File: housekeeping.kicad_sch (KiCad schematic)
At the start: 9 parts, among them U15 LMR43620MSC5RPERQ1

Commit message: Adding control stuff
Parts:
- removed C74: C, symbol Device:C
- removed R72: 49.9k, symbol Device:R_US
- removed R73: 12.4k, symbol Device:R_US
- added C74, C76: 22uF, Capacitor_SMD:CP_Elec_6.3x5.9, symbol Device:C_Polarized_US
- C70: value 0.1uF -> 100nF; footprint (none) -> Capacitor_SMD:C_0603_1608Metric; Mfr (none) -> KYOCERA AVX; Mfr P/N (none) -> 06035C104K4T2A; Supplier_1 (none) -> Digikey; Supplier_1 P/N (none) -> 478-KAM15AR71H104KTTR-ND; Supplier_1 Price @ Qty (none) -> 1; Supplier_1 Unit Price (none) -> 0.10000
- C71: footprint (none) -> Capacitor_SMD:C_0805_2012Metric; Mfr (none) -> Murata Electronics; Mfr P/N (none) -> GCM21BR71H105KA03K; Supplier_1 (none) -> Digikey; Supplier_1 P/N (none) -> 490-13310-2-ND; Supplier_1 Price @ Qty (none) -> 1; Supplier_1 Unit Price (none) -> 0.22000
- C72: footprint (none) -> Capacitor_SMD:C_0805_2012Metric; Mfr (none) -> Murata Electronics; Mfr P/N (none) -> GRT21BR61H475KE13L; Supplier_1 (none) -> Digikey; Supplier_1 P/N (none) -> 490-12394-2-ND; Supplier_1 Price @ Qty (none) -> 1; Supplier_1 Unit Price (none) -> 0.24000
- C73: footprint (none) -> Capacitor_SMD:C_0603_1608Metric; Mfr (none) -> KYOCERA AVX; Mfr P/N (none) -> 06035C104K4T2A; Supplier_1 (none) -> Digikey; Supplier_1 P/N (none) -> 478-KAM15AR71H104KTTR-ND; Supplier_1 Price @ Qty (none) -> 1; Supplier_1 Unit Price (none) -> 0.10000
- L2: footprint (none) -> Inductor_SMD:L_Bourns_SRN6045TA; Mfr (none) -> Bourns Inc.; Mfr P/N (none) -> SRN6045TA-3R3Y; Supplier_1 (none) -> Digikey; Supplier_1 P/N (none) -> SRN6045TA-3R3YTR-ND; Supplier_1 Price @ Qty (none) -> 1; Supplier_1 Unit Price (none) -> 0.45000
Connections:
- net +5V: now also U15.8 (VOUT_BIAS), C74.1, C76.1
- net GND: now also U15.1 (MODE_SYNC), C74.2, C76.2
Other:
- moved on the sheet: C71, C72, L2, U15

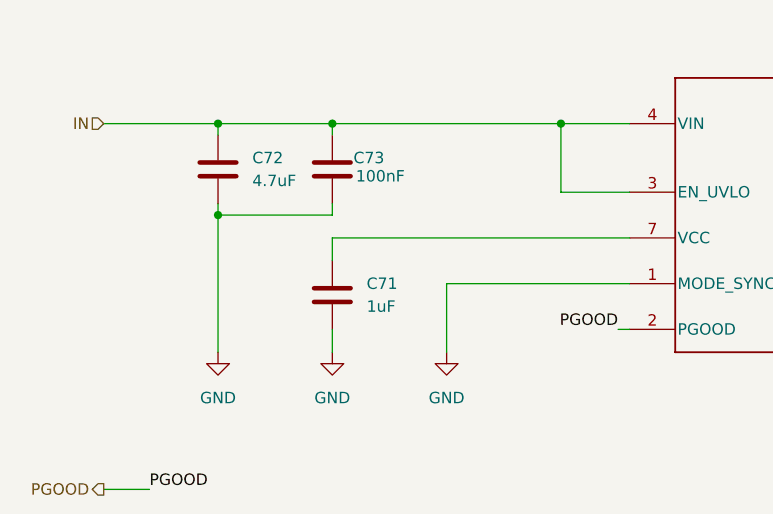
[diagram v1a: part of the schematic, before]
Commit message: Adding in connections to schematic
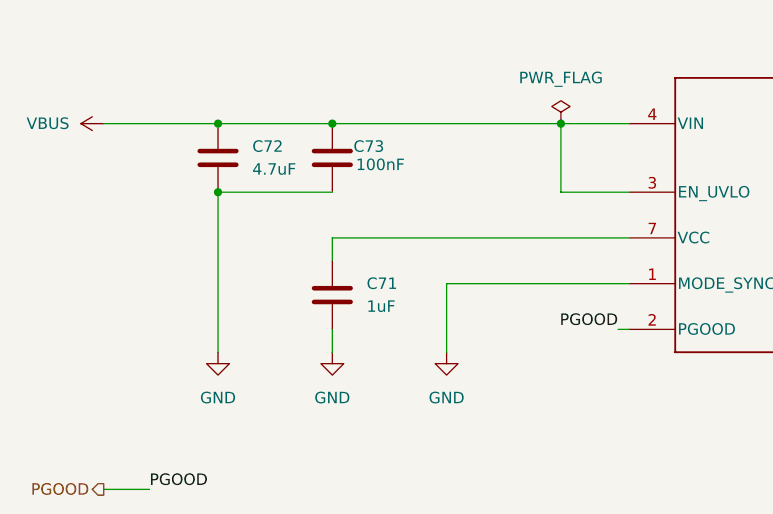
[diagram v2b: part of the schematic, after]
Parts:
- U15: footprint RPE0009A-MFG -> _Power_Board:RPE0009A-MFG
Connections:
- net IN renamed VBUS
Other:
- moved on the sheet: C72, C73
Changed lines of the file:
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@@
+	)
+	(junction
+		(at 58.42 99.06)
+		(diameter 0)
+		(color 0 0 0 0)
 	)
 	(junction
@@
 	)
 	(junction
-		(at 58.42 101.6)
-		(diameter 0)
-		(color 0 0 0 0)
-	)
-	(junction
 		(at 229.87 91.44)
 		(diameter 0)
@@
 	(wire
 		(pts
-			(xy 58.42 100.33) (xy 58.42 101.6)
+			(xy 58.42 99.06) (xy 58.42 116.84)
 		)
 		(stroke
@@
 	(wire
 		(pts
-			(xy 58.42 91.44) (xy 58.42 92.71)
-		)
-		(stroke
-			(width 0)
-			(type default)
-		)
-	)
-	(wire
-		(pts
 			(xy 165.1 114.3) (xy 172.72 114.3)
 		)
@@
 	(wire
 		(pts
-			(xy 58.42 101.6) (xy 58.42 116.84)
-		)
-		(stroke
-			(width 0)
-			(type default)
-		)
-	)
-	(wire
-		(pts
 			(xy 45.72 91.44) (xy 58.42 91.44)
 		)
@@
 	(wire
 		(pts
-			(xy 71.12 101.6) (xy 71.12 100.33)
-		)
-		(stroke
-			(width 0)
-			(type default)
-		)
-	)
-	(wire
-		(pts
 			(xy 203.2 91.44) (xy 217.17 91.44)
 		)
@@
 	(wire
 		(pts
-			(xy 58.42 101.6) (xy 71.12 101.6)
-		)
-		(stroke
-			(width 0)
-			(type default)
-		)
-	)
-	(wire
-		(pts
-			(xy 71.12 91.44) (xy 71.12 92.71)
+			(xy 58.42 99.06) (xy 71.12 99.06)
 		)
 		(stroke
@@
 			)
 			(justify left bottom)
-		)
-	)
-	(hierarchical_label "IN"
-		(shape input)
-		(at 45.72 91.44 180)
-		(effects
-			(font
-				(size 1.27 1.27)
-			)
-			(justify right)
 		)
 	)
@@
 			)
 		)
-		(property "Footprint" "RPE0009A-MFG"
+		(property "Footprint" "_Power_Board:RPE0009A-MFG"
 			(at 104.14 91.44 0)
 			(effects
@@
 	)
 	(symbol
+		(lib_id "power:PWR_FLAG")
+		(at 96.52 91.44 0)
+		(unit 1)
+		(exclude_from_sim no)
+		(in_bom yes)
+		(on_board yes)
+		(dnp no)
+		(fields_autoplaced yes)
+		(property "Reference" "#FLG01"
+			(at 96.52 89.535 0)
+			(effects
+				(font
+					(size 1.27 1.27)
+				)
+				(hide yes)
+			)
+		)
+		(property "Value" "PWR_FLAG"
+			(at 96.52 86.36 0)
+			(effects
+				(font
+					(size 1.27 1.27)
+				)
+			)
+		)
+		(property "Footprint" ""
+			(at 96.52 91.44 0)
+			(effects
+				(font
+					(size 1.27 1.27)
+				)
+				(hide yes)
+			)
+		)
+		(property "Datasheet" "~"
+			(at 96.52 91.44 0)
+			(effects
+				(font
+					(size 1.27 1.27)
+				)
+				(hide yes)
+			)
+		)
+		(property "Description" "Special symbol for telling ERC where power comes from"
+			(at 96.52 91.44 0)
+			(effects
+				(font
+					(size 1.27 1.27)
+				)
+				(hide yes)
+			)
+		)
+		(pin "1"
+		)
+		(instances
+			(project ""
+				(path "/99785679-20de-4827-b4cc-bc3c187068c9/9564929a-642e-4163-88c2-45054b63a5ed/82ef1b6a-46bf-4ed0-b9a8-2180f415726a"
+					(reference "#FLG01")
+					(unit 1)
+				)
+			)
+		)
+	)
+	(symbol
 		(lib_id "Device:C_Polarized_US")
 		(at 229.87 96.52 0)
@@
 	(symbol
 		(lib_id "Device:C")
-		(at 71.12 96.52 0)
+		(at 71.12 95.25 0)
 		(unit 1)
 		(exclude_from_sim no)
@@
 		(dnp no)
 		(property "Reference" "C73"
-			(at 75.184 95.25 0)
+			(at 75.184 93.98 0)
 			(effects
 				(font
@@
 		)
 		(property "Value" "100nF"
-			(at 76.454 97.282 0)
+			(at 76.454 96.012 0)
 			(effects
 				(font
@@
 		)
 		(property "Footprint" "Capacitor_SMD:C_0603_1608Metric"
-			(at 72.0852 100.33 0)
+			(at 72.0852 99.06 0)
 			(effects
 				(font
@@
 		)
 		(property "Datasheet" "https://datasheets.kyocera-avx.com/AutoMLCC.pdf"
-			(at 71.12 96.52 0)
+			(at 71.12 95.25 0)
 			(effects
 				(font
@@
 		)
 		(property "Description" "CAP CER 0.1UF 50V X7R 0603"
-			(at 71.12 96.52 0)
+			(at 71.12 95.25 0)
 			(effects
 				(font
@@
 		)
 		(property "Mfr" "KYOCERA AVX"
-			(at 71.12 96.52 0)
+			(at 71.12 95.25 0)
 			(effects
 				(font
@@
 		)
 		(property "Mfr P/N" "06035C104K4T2A"
-			(at 71.12 96.52 0)
+			(at 71.12 95.25 0)
 			(effects
 				(font
@@
 		)
 		(property "Supplier_1" "Digikey"
-			(at 71.12 96.52 0)
+			(at 71.12 95.25 0)
 			(effects
 				(font
@@
 		)
 		(property "Supplier_1 P/N" "478-KAM15AR71H104KTTR-ND"
-			(at 71.12 96.52 0)
+			(at 71.12 95.25 0)
 			(effects
 				(font
@@
 		)
 		(property "Supplier_1 Unit Price" "0.10000"
-			(at 71.12 96.52 0)
+			(at 71.12 95.25 0)
 			(effects
 				(font
@@
 		)
 		(property "Supplier_1 Price @ Qty" "1"
-			(at 71.12 96.52 0)
+			(at 71.12 95.25 0)
 			(effects
 				(font
@@
 		)
 		(property "Supplier_2" ""
-			(at 71.12 96.52 0)
+			(at 71.12 95.25 0)
 			(effects
 				(font
@@
 		)
 		(property "Supplier_2 P/N" ""
-			(at 71.12 96.52 0)
+			(at 71.12 95.25 0)
 			(effects
 				(font
@@
 		)
 		(property "Supplier_2 Unit Price" ""
-			(at 71.12 96.52 0)
+			(at 71.12 95.25 0)
 			(effects
 				(font
@@
 		)
 		(property "Supplier_2 Price @ Qty" ""
-			(at 71.12 96.52 0)
+			(at 71.12 95.25 0)
 			(effects
 				(font
@@
 	(symbol
 		(lib_id "Device:C")
-		(at 58.42 96.52 0)
+		(at 58.42 95.25 0)
 		(unit 1)
 		(exclude_from_sim no)
@@
 		(fields_autoplaced yes)
 		(property "Reference" "C72"
-			(at 62.23 95.2499 0)
+			(at 62.23 93.9799 0)
 			(effects
 				(font
@@
 		)
 		(property "Value" "4.7uF"
-			(at 62.23 97.7899 0)
+			(at 62.23 96.5199 0)
 			(effects
 				(font
@@
 		)
 		(property "Footprint" "Capacitor_SMD:C_0805_2012Metric"
-			(at 59.3852 100.33 0)
+			(at 59.3852 99.06 0)
 			(effects
 				(font
@@
 		)
 		(property "Datasheet" "https://search.murata.co.jp/Ceramy/image/img/A01X/G101/ENG/GRT21BR61H475KE13-01.pdf"
-			(at 58.42 96.52 0)
+			(at 58.42 95.25 0)
 			(effects
 				(font
@@
 		)
 		(property "Description" "CAP CER 4.7UF 50V X5R 0805"
-			(at 58.42 96.52 0)
+			(at 58.42 95.25 0)
 			(effects
 				(font
@@
 		)
 		(property "Mfr" "Murata Electronics"
-			(at 58.42 96.52 0)
+			(at 58.42 95.25 0)
 			(effects
 				(font
@@
 		)
 		(property "Mfr P/N" "GRT21BR61H475KE13L"
-			(at 58.42 96.52 0)
+			(at 58.42 95.25 0)
 			(effects
 				(font
@@
 		)
 		(property "Supplier_1" "Digikey"
-			(at 58.42 96.52 0)
+			(at 58.42 95.25 0)
 			(effects
 				(font
@@
 		)
 		(property "Supplier_1 P/N" "490-12394-2-ND"
-			(at 58.42 96.52 0)
+			(at 58.42 95.25 0)
 			(effects
 				(font
@@
 		)
 		(property "Supplier_1 Unit Price" "0.24000"
-			(at 58.42 96.52 0)
+			(at 58.42 95.25 0)
 			(effects
 				(font
@@
 		)
 		(property "Supplier_1 Price @ Qty" "1"
-			(at 58.42 96.52 0)
+			(at 58.42 95.25 0)
 			(effects
 				(font
@@
 		)
 		(property "Supplier_2" ""
-			(at 58.42 96.52 0)
+			(at 58.42 95.25 0)
 			(effects
 				(font
@@
 		)
 		(property "Supplier_2 P/N" ""
-			(at 58.42 96.52 0)
+			(at 58.42 95.25 0)
 			(effects
 				(font
@@
 		)
 		(property "Supplier_2 Unit Price" ""
-			(at 58.42 96.52 0)
+			(at 58.42 95.25 0)
 			(effects
 				(font
@@
 		)
 		(property "Supplier_2 Price @ Qty" ""
-			(at 58.42 96.52 0)
+			(at 58.42 95.25 0)
 			(effects
 				(font
@@
 					(unit 1)
 				)
+			)
+		)
+	)
+	(symbol
+		(lib_id "power:VBUS")
+		(at 45.72 91.44 90)
+		(unit 1)
+		(exclude_from_sim no)
+		(in_bom yes)
+		(on_board yes)
+		(dnp no)
+		(fields_autoplaced yes)
+		(property "Reference" "#PWR0134"
+			(at 49.53 91.44 0)
+			(effects
+				(font
+					(size 1.27 1.27)
+				)
+				(hide yes)
+			)
+		)
+		(property "Value" "VBUS"
+			(at 41.91 91.4399 90)
+			(effects
+				(font
+					(size 1.27 1.27)
+				)
+				(justify left)
+			)
+		)
+		(property "Footprint" ""
+			(at 45.72 91.44 0)
+			(effects
+				(font
+					(size 1.27 1.27)
+				)
+				(hide yes)
+			)
+		)
+		(property "Datasheet" ""
+			(at 45.72 91.44 0)
+			(effects
+				(font
+					(size 1.27 1.27)
+				)
+				(hide yes)
+			)
+		)
+		(property "Description" "Power symbol creates a global label with name \"VBUS\""
+			(at 45.72 91.44 0)
+			(effects
+				(font
+					(size 1.27 1.27)
+				)
+				(hide yes)
+			)
+		)
+		(pin "1"
+		)
+		(instances
+			(project ""
+				(path "/99785679-20de-4827-b4cc-bc3c187068c9/9564929a-642e-4163-88c2-45054b63a5ed/82ef1b6a-46bf-4ed0-b9a8-2180f415726a"
+					(reference "#PWR0134")
+					(unit 1)
+				)

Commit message: Working on layout now
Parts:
- renumbered C72 to C80, C73 to C81, C71 to C82, C70 to C83, C76 to C84, C74 to C85, L2 to L3, U15 to U18
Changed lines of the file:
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@@
 		(dnp no)
 		(fields_autoplaced yes)
-		(property "Reference" "#PWR0117"
+		(property "Reference" "#PWR0133"
 			(at 172.72 123.19 0)
 			(effects
@@
 			(project ""
 				(path "/99785679-20de-4827-b4cc-bc3c187068c9/9564929a-642e-4163-88c2-45054b63a5ed/82ef1b6a-46bf-4ed0-b9a8-2180f415726a"
-					(reference "#PWR0117")
+					(reference "#PWR0133")
 					(unit 1)
 				)
@@
 		(dnp no)
 		(fields_autoplaced yes)
-		(property "Reference" "U15"
+		(property "Reference" "U18"
 			(at 134.62 81.28 0)
 			(effects
@@
 			(project ""
 				(path "/99785679-20de-4827-b4cc-bc3c187068c9/9564929a-642e-4163-88c2-45054b63a5ed/82ef1b6a-46bf-4ed0-b9a8-2180f415726a"
-					(reference "U15")
+					(reference "U18")
 					(unit 1)
 				)
@@
 		(on_board yes)
 		(dnp no)
-		(property "Reference" "C76"
+		(property "Reference" "C84"
 			(at 219.456 95.25 0)
 			(effects
@@
 			(project ""
 				(path "/99785679-20de-4827-b4cc-bc3c187068c9/9564929a-642e-4163-88c2-45054b63a5ed/82ef1b6a-46bf-4ed0-b9a8-2180f415726a"
-					(reference "C76")
+					(reference "C84")
 					(unit 1)
 				)
@@
 		(dnp no)
 		(fields_autoplaced yes)
-		(property "Reference" "#PWR0122"
+		(property "Reference" "#PWR0134"
 			(at 223.52 123.19 0)
 			(effects
@@
 			(project "PowerBoard"
 				(path "/99785679-20de-4827-b4cc-bc3c187068c9/9564929a-642e-4163-88c2-45054b63a5ed/82ef1b6a-46bf-4ed0-b9a8-2180f415726a"
-					(reference "#PWR0122")
+					(reference "#PWR0134")
 					(unit 1)
 				)
@@
 		(dnp no)
 		(fields_autoplaced yes)
-		(property "Reference" "#PWR0118"
+		(property "Reference" "#PWR0131"
 			(at 71.12 123.19 0)
 			(effects
@@
 			(project "PowerBoard"
 				(path "/99785679-20de-4827-b4cc-bc3c187068c9/9564929a-642e-4163-88c2-45054b63a5ed/82ef1b6a-46bf-4ed0-b9a8-2180f415726a"
-					(reference "#PWR0118")
+					(reference "#PWR0131")
 					(unit 1)
 				)
@@
 		(dnp no)
 		(fields_autoplaced yes)
-		(property "Reference" "#PWR0121"
+		(property "Reference" "#PWR0132"
 			(at 83.82 123.19 0)
 			(effects
@@
 			(project "PowerBoard"
 				(path "/99785679-20de-4827-b4cc-bc3c187068c9/9564929a-642e-4163-88c2-45054b63a5ed/82ef1b6a-46bf-4ed0-b9a8-2180f415726a"
-					(reference "#PWR0121")
+					(reference "#PWR0132")
 					(unit 1)
 				)
@@
 		(dnp no)
 		(fields_autoplaced yes)
-		(property "Reference" "L2"
+		(property "Reference" "L3"
 			(at 187.96 86.36 90)
 			(effects
@@
 			(project ""
 				(path "/99785679-20de-4827-b4cc-bc3c187068c9/9564929a-642e-4163-88c2-45054b63a5ed/82ef1b6a-46bf-4ed0-b9a8-2180f415726a"
-					(reference "L2")
+					(reference "L3")
 					(unit 1)
 				)
@@
 		(dnp no)
 		(fields_autoplaced yes)
-		(property "Reference" "#FLG01"
+		(property "Reference" "#FLG014"
 			(at 96.52 89.535 0)
 			(effects
@@
 			(project ""
 				(path "/99785679-20de-4827-b4cc-bc3c187068c9/9564929a-642e-4163-88c2-45054b63a5ed/82ef1b6a-46bf-4ed0-b9a8-2180f415726a"
-					(reference "#FLG01")
+					(reference "#FLG014")
 					(unit 1)
 				)
@@
 		(on_board yes)
 		(dnp no)
-		(property "Reference" "C74"
+		(property "Reference" "C85"
 			(at 232.156 95.25 0)
 			(effects
@@
 			(project "PowerBoard"
 				(path "/99785679-20de-4827-b4cc-bc3c187068c9/9564929a-642e-4163-88c2-45054b63a5ed/82ef1b6a-46bf-4ed0-b9a8-2180f415726a"
-					(reference "C74")
+					(reference "C85")
 					(unit 1)
 				)
@@
 		(dnp no)
 		(fields_autoplaced yes)
-		(property "Reference" "C71"
+		(property "Reference" "C82"
 			(at 74.93 109.2199 0)
 			(effects
@@
 			(project ""
 				(path "/99785679-20de-4827-b4cc-bc3c187068c9/9564929a-642e-4163-88c2-45054b63a5ed/82ef1b6a-46bf-4ed0-b9a8-2180f415726a"
-					(reference "C71")
+					(reference "C82")
 					(unit 1)
 				)
@@
 		(on_board yes)
 		(dnp no)
-		(property "Reference" "C73"
+		(property "Reference" "C81"
 			(at 75.184 93.98 0)
 			(effects
@@
 			(project "PowerBoard"
 				(path "/99785679-20de-4827-b4cc-bc3c187068c9/9564929a-642e-4163-88c2-45054b63a5ed/82ef1b6a-46bf-4ed0-b9a8-2180f415726a"
-					(reference "C73")
+					(reference "C81")
 					(unit 1)
 				)
@@
 		(dnp no)
 		(fields_autoplaced yes)
-		(property "Reference" "#PWR0119"
+		(property "Reference" "#PWR0130"
 			(at 58.42 123.19 0)
 			(effects
@@
 			(project "PowerBoard"
 				(path "/99785679-20de-4827-b4cc-bc3c187068c9/9564929a-642e-4163-88c2-45054b63a5ed/82ef1b6a-46bf-4ed0-b9a8-2180f415726a"
-					(reference "#PWR0119")
+					(reference "#PWR0130")
 					(unit 1)
 				)
@@
 		(dnp no)
 		(fields_autoplaced yes)
-		(property "Reference" "#PWR0120"
+		(property "Reference" "#PWR0135"
 			(at 246.38 91.44 0)
 			(effects
@@
 			(project ""
 				(path "/99785679-20de-4827-b4cc-bc3c187068c9/9564929a-642e-4163-88c2-45054b63a5ed/82ef1b6a-46bf-4ed0-b9a8-2180f415726a"
-					(reference "#PWR0120")
+					(reference "#PWR0135")
 					(unit 1)
 				)
@@
 		(on_board yes)
 		(dnp no)
-		(property "Reference" "C70"
+		(property "Reference" "C83"
 			(at 176.784 93.98 0)
 			(effects
@@
 			(project "PowerBoard"
 				(path "/99785679-20de-4827-b4cc-bc3c187068c9/9564929a-642e-4163-88c2-45054b63a5ed/82ef1b6a-46bf-4ed0-b9a8-2180f415726a"
-					(reference "C70")
+					(reference "C83")
 					(unit 1)
 				)
@@
 		(dnp no)
 		(fields_autoplaced yes)
-		(property "Reference" "C72"
+		(property "Reference" "C80"
 			(at 62.23 93.9799 0)
 			(effects
@@
 			(project ""
 				(path "/99785679-20de-4827-b4cc-bc3c187068c9/9564929a-642e-4163-88c2-45054b63a5ed/82ef1b6a-46bf-4ed0-b9a8-2180f415726a"
-					(reference "C72")
+					(reference "C80")
 					(unit 1)
 				)
@@
 		(dnp no)
 		(fields_autoplaced yes)
-		(property "Reference" "#PWR0134"
+		(property "Reference" "#PWR0129"
 			(at 49.53 91.44 0)
 			(effects
@@
 			(project ""
 				(path "/99785679-20de-4827-b4cc-bc3c187068c9/9564929a-642e-4163-88c2-45054b63a5ed/82ef1b6a-46bf-4ed0-b9a8-2180f415726a"
-					(reference "#PWR0134")
+					(reference "#PWR0129")
 					(unit 1)
 				)

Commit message: BOM in folder
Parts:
- C80: Supplier_1 Digikey -> LCSC; Supplier_1 P/N 490-12394-2-ND -> C437576; Supplier_1 Unit Price 0.24000 -> (none)
- C81, C83: JLCPCB Status (none) -> JLC in-stock package match; Mfr P/N 06035C104K4T2A -> CC0603KRX7R9BB104; Supplier_1 Digikey -> LCSC; Supplier_1 P/N 478-KAM15AR71H104KTTR-ND -> C14663; Supplier_1 Unit Price 0.10000 -> (none)
- C82: Supplier_1 Digikey -> LCSC; Supplier_1 P/N 490-13310-2-ND -> C576424; Supplier_1 Unit Price 0.22000 -> (none)
- C84, C85: Supplier_1 Digikey -> LCSC; Supplier_1 P/N P15463TR-ND -> C178643; Supplier_1 Unit Price 0.83000 -> (none)
- L3: Supplier_1 Digikey -> LCSC; Supplier_1 P/N SRN6045TA-3R3YTR-ND -> C3221229; Supplier_1 Unit Price 0.45000 -> (none)
- U18: Supplier_1 Digikey -> LCSC; Supplier_1 P/N 296-LMR43620MSC5RPERQ1TR-ND -> C6979910; Supplier_1 Unit Price 3.81000 -> (none)
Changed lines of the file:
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@@
 			)
 		)
-		(property "Supplier_1" "Digikey"
+		(property "Supplier_1" "LCSC"
 			(at 104.14 91.44 0)
 			(effects
@@
 			)
 		)
-		(property "Supplier_1 P/N" "296-LMR43620MSC5RPERQ1TR-ND"
+		(property "Supplier_1 P/N" "C6979910"
 			(at 104.14 91.44 0)
 			(effects
@@
 			)
 		)
-		(property "Supplier_1 Unit Price" "3.81000"
+		(property "Supplier_1 Unit Price" ""
 			(at 104.14 91.44 0)
 			(effects
@@
 			)
 		)
-		(property "Supplier_1" "Digikey"
+		(property "Supplier_1" "LCSC"
 			(at 217.17 96.52 0)
 			(effects
@@
 			)
 		)
-		(property "Supplier_1 P/N" "P15463TR-ND"
+		(property "Supplier_1 P/N" "C178643"
 			(at 217.17 96.52 0)
 			(effects
@@
 			)
 		)
-		(property "Supplier_1 Unit Price" "0.83000"
+		(property "Supplier_1 Unit Price" ""
 			(at 217.17 96.52 0)
 			(effects
@@
 			)
 		)
-		(property "Supplier_1" "Digikey"
+		(property "Supplier_1" "LCSC"
 			(at 187.96 91.44 0)
 			(effects
@@
 			)
 		)
-		(property "Supplier_1 P/N" "SRN6045TA-3R3YTR-ND"
+		(property "Supplier_1 P/N" "C3221229"
 			(at 187.96 91.44 0)
 			(effects
@@
 			)
 		)
-		(property "Supplier_1 Unit Price" "0.45000"
+		(property "Supplier_1 Unit Price" ""
 			(at 187.96 91.44 0)
 			(effects
@@
 			)
 		)
-		(property "Supplier_1" "Digikey"
+		(property "Supplier_1" "LCSC"
 			(at 229.87 96.52 0)
 			(effects
@@
 			)
 		)
-		(property "Supplier_1 P/N" "P15463TR-ND"
+		(property "Supplier_1 P/N" "C178643"
 			(at 229.87 96.52 0)
 			(effects
@@
 			)
 		)
-		(property "Supplier_1 Unit Price" "0.83000"
+		(property "Supplier_1 Unit Price" ""
 			(at 229.87 96.52 0)
 			(effects
@@
 			)
 		)
-		(property "Supplier_1" "Digikey"
+		(property "Supplier_1" "LCSC"
 			(at 71.12 110.49 0)
 			(effects
@@
 			)
 		)
-		(property "Supplier_1 P/N" "490-13310-2-ND"
+		(property "Supplier_1 P/N" "C576424"
 			(at 71.12 110.49 0)
 			(effects
@@
 			)
 		)
-		(property "Supplier_1 Unit Price" "0.22000"
+		(property "Supplier_1 Unit Price" ""
 			(at 71.12 110.49 0)
 			(effects
@@
 			)
 		)
-		(property "Mfr P/N" "06035C104K4T2A"
+		(property "Mfr P/N" "CC0603KRX7R9BB104"
 			(at 71.12 95.25 0)
 			(effects
@@
 			)
 		)
-		(property "Supplier_1" "Digikey"
+		(property "Supplier_1" "LCSC"
 			(at 71.12 95.25 0)
 			(effects
@@
 			)
 		)
-		(property "Supplier_1 P/N" "478-KAM15AR71H104KTTR-ND"
+		(property "Supplier_1 P/N" "C14663"
 			(at 71.12 95.25 0)
 			(effects
@@
 			)
 		)
-		(property "Supplier_1 Unit Price" "0.10000"
+		(property "Supplier_1 Unit Price" ""
 			(at 71.12 95.25 0)
 			(effects
@@
 		)
 		(property "Supplier_2 Price @ Qty" ""
+			(at 71.12 95.25 0)
+			(effects
+				(font
+					(size 1.27 1.27)
+				)
+				(hide yes)
+			)
+		)
+		(property "JLCPCB Status" "JLC in-stock package match"
 			(at 71.12 95.25 0)
 			(effects
@@
 			)
 		)
-		(property "Mfr P/N" "06035C104K4T2A"
+		(property "Mfr P/N" "CC0603KRX7R9BB104"
 			(at 172.72 95.25 0)
 			(effects
@@
 			)
 		)
-		(property "Supplier_1" "Digikey"
+		(property "Supplier_1" "LCSC"
 			(at 172.72 95.25 0)
 			(effects
@@
 			)
 		)
-		(property "Supplier_1 P/N" "478-KAM15AR71H104KTTR-ND"
+		(property "Supplier_1 P/N" "C14663"
 			(at 172.72 95.25 0)
 			(effects
@@
 			)
 		)
-		(property "Supplier_1 Unit Price" "0.10000"
+		(property "Supplier_1 Unit Price" ""
 			(at 172.72 95.25 0)
 			(effects
@@
 		)
 		(property "Supplier_2 Price @ Qty" ""
+			(at 172.72 95.25 0)
+			(effects
+				(font
+					(size 1.27 1.27)
+				)
+				(hide yes)
+			)
+		)
+		(property "JLCPCB Status" "JLC in-stock package match"
 			(at 172.72 95.25 0)
 			(effects
@@
 			)
 		)
-		(property "Supplier_1" "Digikey"
+		(property "Supplier_1" "LCSC"
 			(at 58.42 95.25 0)
 			(effects
@@
 			)
 		)
-		(property "Supplier_1 P/N" "490-12394-2-ND"
+		(property "Supplier_1 P/N" "C437576"
 			(at 58.42 95.25 0)
 			(effects
@@
 			)
 		)
-		(property "Supplier_1 Unit Price" "0.24000"
+		(property "Supplier_1 Unit Price" ""
 			(at 58.42 95.25 0)
 			(effects
